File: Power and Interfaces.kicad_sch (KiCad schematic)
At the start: 32 parts, among them J3 Molex 43650-0500, J4 Molex 43650-0500, U4 TPS54302, U5 TLV74033PDBVR

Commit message: more schematic work and initial layout
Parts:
- removed D8: D_Schottky, Diode_SMD:D_SMA, symbol Device:D_Schottky
- added D16: D_Schottky, Diode_SMD:D_SOD-123F, symbol Device:D_Schottky
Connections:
- net +12V: now also D16.1 (K)
- net +12V_LOCAL: now also D16.2 (A)

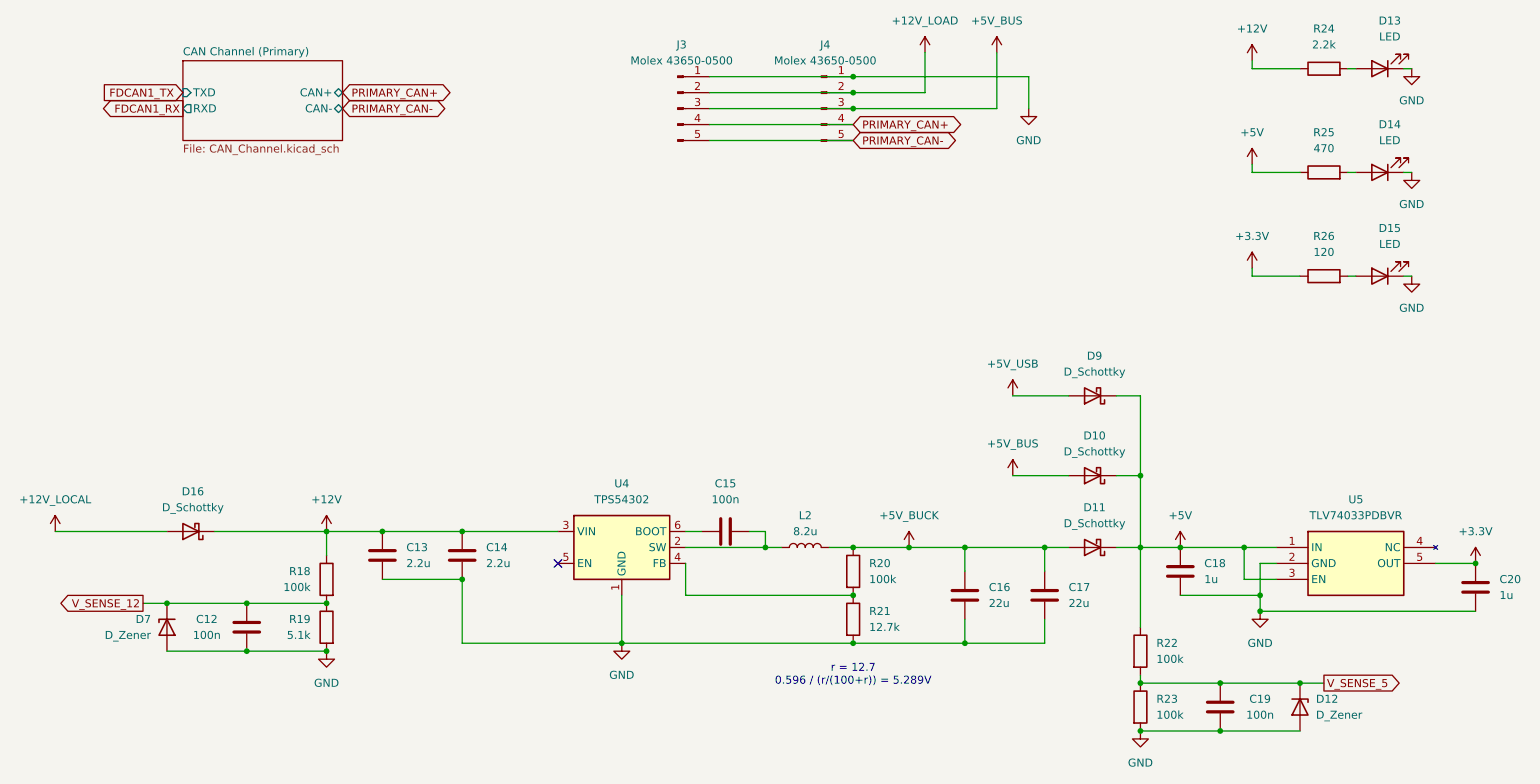
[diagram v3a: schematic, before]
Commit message: finished layout, routing, and silkscreen
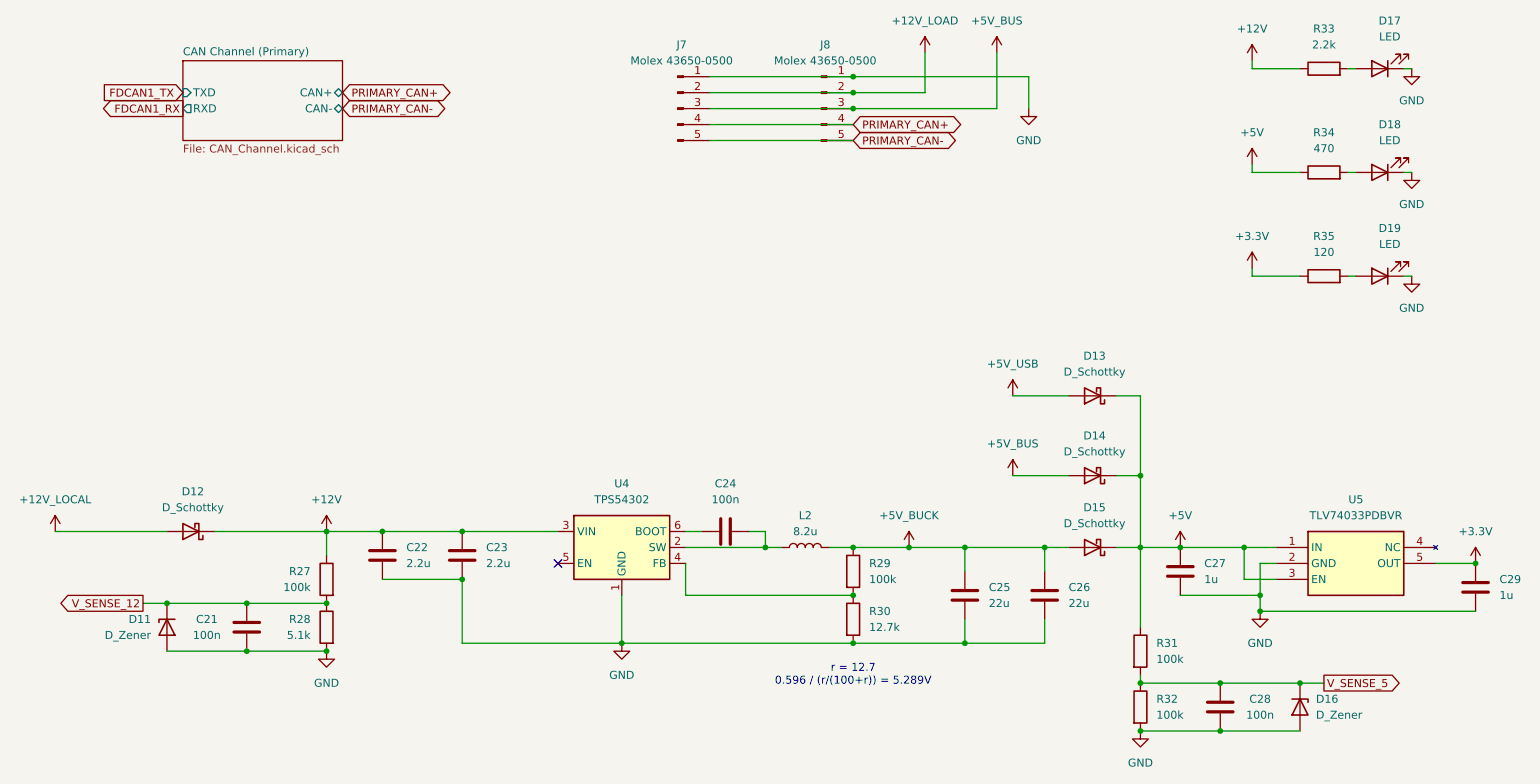
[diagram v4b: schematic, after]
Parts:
- renumbered C12 to C21, C13 to C22, C14 to C23, C15 to C24, C16 to C25, C17 to C26, C18 to C27, C19 to C28, C20 to C29, D7 to D11, D16 to D12, D9 to D13, D10 to D14, D11 to D15, D12 to D16, D13 to D17, D14 to D18, D15 to D19, J3 to J7, J4 to J8, R18 to R27, R19 to R28, R20 to R29, R21 to R30, R22 to R31, R23 to R32, R24 to R33, R25 to R34, R26 to R35

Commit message: r0 final
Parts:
- removed D11, D16: D_Zener, Diode_SMD:D_SOD-323_HandSoldering, symbol Device:D_Zener
- renumbered D14 to D10, D15 to D11, D17 to D12, D18 to D13, D19 to D14, D12 to D8, D13 to D9, J7 to J8, J8 to J9
